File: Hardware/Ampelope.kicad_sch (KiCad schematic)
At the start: 44 parts, among them J1 Gate1_In, J3 Eurorack_10_pin_power, J4 Audio1_Out, U1 TL074

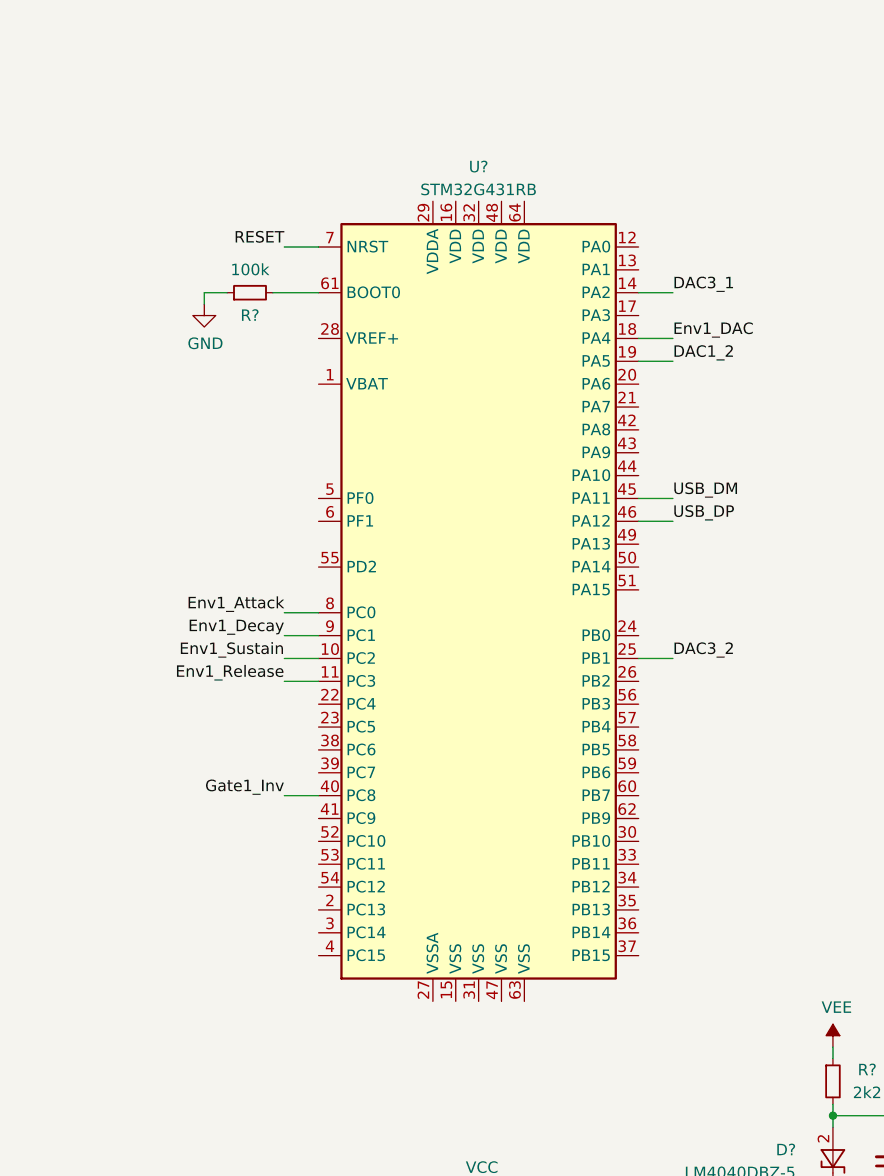
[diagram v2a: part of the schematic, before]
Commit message: Added power supply components to schematic
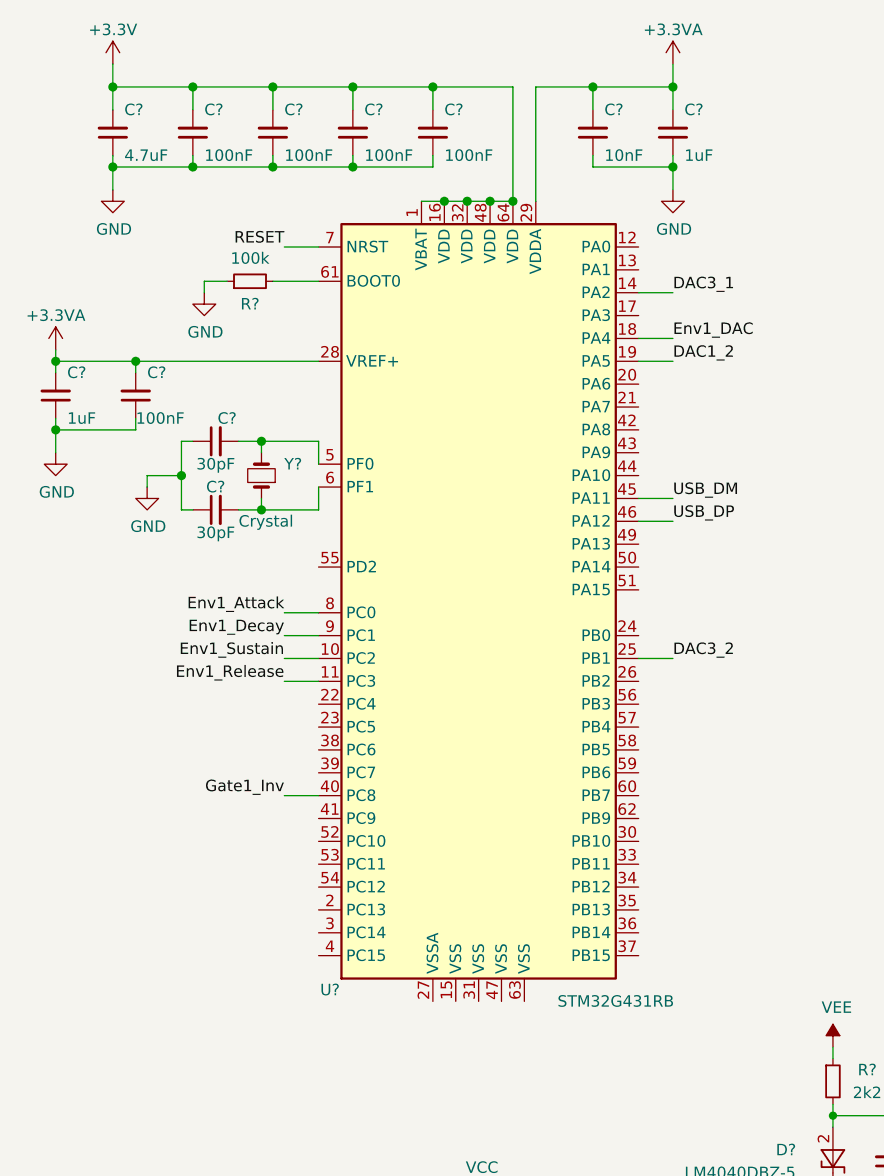
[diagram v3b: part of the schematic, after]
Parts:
- added C? (x5): 100nF, symbol Device:C_Small
- added C? (x2): 1uF, symbol Device:C_Small
- added C? (x2): 30pF, symbol Device:C_Small
- added C?: 10nF, symbol Device:C_Small
- added C?: 4.7uF, symbol Device:C_Small
- added Y?: Crystal, symbol Device:Crystal_Small
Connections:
- net +3.3VA: now also U?.28 (VREF+), U?.29 (VDDA), C?.2, C?.2, C?.2, C?.2
- net +3V3: now also U?.1 (VBAT), U?.16 (VDD), U?.32 (VDD), U?.48 (VDD), U?.64 (VDD), C?.2, C?.2, C?.2, C?.2, C?.2
- net GND: now also C?.1, C?.1, C?.1, C?.1, C?.1, C?.1, C?.1, C?.1, C?.1, C?.1, C?.1
- net at U?.5 (PF0): now also C?.2, Y?.2
- net at U?.6 (PF1): now also C?.2, Y?.1
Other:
- moved on the sheet: R?

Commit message: Duplicated IO for all four envelopes/VCAs
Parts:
- removed C?: 100nF, Capacitors_SMD:C_0603_HandSoldering, symbol Device:C_Small
- removed D?: LM4040DBZ-5, TO_SOT_Packages_SMD:SOT-23, symbol Reference_Voltage:LM4040DBZ-10
- removed J?: Audio1_In, Custom_Footprints:THONKICONN_hole, symbol thonkiconn:AudioJack2_Ground_Switch
- removed R? (x2): 10k, Resistors_SMD:R_0603_HandSoldering, symbol Device:R_Small
- removed R?: 2k2, Resistors_SMD:R_0603_HandSoldering, symbol Device:R_Small
- removed unit 1 of U1
- added C? (x3): 100pF, symbol Device:C_Small
- added D? (x3): LED, symbol Device:LED
- added J?: Audio1_In, Custom_Footprints:THONKICONN_hole, symbol thonkiconn:AudioJack2_Ground_Switch
- added J?: Audio2_In, Custom_Footprints:THONKICONN_hole, symbol thonkiconn:AudioJack2_Ground_Switch
- added J?: Audio4_Out, Custom_Footprints:THONKICONN_hole, symbol thonkiconn:AudioJack2_Ground_Switch
- added J?: Env3_Out, Custom_Footprints:THONKICONN_hole, symbol thonkiconn:AudioJack2_Ground_Switch
- added J?: Gate4_In, Custom_Footprints:THONKICONN_hole, symbol thonkiconn:AudioJack2_Ground_Switch
- added J?: Audio4_In, Custom_Footprints:THONKICONN_hole, symbol thonkiconn:AudioJack2_Ground_Switch
- added J?: Audio3_In, Custom_Footprints:THONKICONN_hole, symbol thonkiconn:AudioJack2_Ground_Switch
- added J?: Gate2_In, Custom_Footprints:THONKICONN_hole, symbol thonkiconn:AudioJack2_Ground_Switch
- added J?: Audio3_Out, Custom_Footprints:THONKICONN_hole, symbol thonkiconn:AudioJack2_Ground_Switch
- added J?: Env4_Out, Custom_Footprints:THONKICONN_hole, symbol thonkiconn:AudioJack2_Ground_Switch
- added J?: Env2_Out, Custom_Footprints:THONKICONN_hole, symbol thonkiconn:AudioJack2_Ground_Switch
- added J?: Audio2_Out, Custom_Footprints:THONKICONN_hole, symbol thonkiconn:AudioJack2_Ground_Switch
- added J?: Gate3_In, Custom_Footprints:THONKICONN_hole, symbol thonkiconn:AudioJack2_Ground_Switch
- added Q? (x3): 2N3904, Package_TO_SOT_THT:TO-92_Inline, symbol Transistor_BJT:2N3904
- added R? (x10): 1k, Resistors_SMD:R_0603_HandSoldering, symbol Device:R_Small
- added R? (x8): 10k, Resistors_SMD:R_0603_HandSoldering, symbol Device:R_Small
- added R? (x3): 30k, Resistors_SMD:R_0603_HandSoldering, symbol Device:R_Small
- added R? (x3): 75k, Resistors_SMD:R_0603_HandSoldering, symbol Device:R
- added R? (x3): 1k, Resistors_SMD:R_0603_HandSoldering, symbol Device:R
- added R? (x3): 20k, Resistors_SMD:R_0603_HandSoldering, symbol Device:R
- added R? (x3): 47k, Resistors_SMD:R_0603_HandSoldering, symbol Device:R
- added SW?: SW_SP3T, symbol Switch:SW_SP3T
- added U? (x12): TL074, Package_SO:SOIC-14_3.9x8.7mm_P1.27mm, symbol Amplifier_Operational:TL074
- J?: value Audio1_Out -> Env1_Out
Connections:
- net +3V3: now also R?.2, R?.2, R?.2
- net Audio1_In_Buff: now also R?.1, U?.1
- net Audio1_VCA: now also U1.2 (-); no longer U1.6 (-)
- net Audio2_In_Buff: now also R?.1, U?.7
- net Audio2_VCA: now also C?.1, R?.2, U?.6 (-)
- net Audio3_In_Buff: now also R?.1, U?.8
- net Audio3_VCA: now also C?.1, R?.2, U?.9 (-)
- net Audio4_In_Buff: now also R?.1, U?.14
- net Audio4_VCA: now also C?.1, R?.2, U?.13 (-)
- net DAC1_2: no longer U?.19 (PA5)
- net DAC3_1: no longer U?.14 (PA2)
- net DAC3_2: no longer U?.25 (PB1)
- net GND: now also U1.3 (+), U1.3 (+), U?.15 (VSS), U?.27 (VSSA), U?.31 (VSS), U?.47 (VSS), U?.63 (VSS), J?.1, J?.1, J?.1, J?.1, J?.1, J?.1, J?.1, J?.1, J?.1, J?.1, J?.1, J?.1, J?.1, J?.2, J?.2, J?.2, J?.2, J?.3, J?.3, J?.3, J?.3, Q?.1 (E), Q?.1 (E), Q?.1 (E), R?.2, R?.2, R?.2, R?.2, R?.2, R?.2, R?.2, U?.10 (+), U?.10 (+), U?.10 (+), U?.12 (+), U?.12 (+), U?.12 (+), U?.3 (+), U?.5 (+), U?.5 (+), U?.5 (+); no longer U1.10 (+), U1.5 (+)
- net VCC: now also U?.4 (V+), U?.4 (V+)
- net VEE: now also R?.2, R?.2, R?.2, U?.11 (V-), U?.11 (V-)
- net Gate1: now reaches J1.3, R?.1
- net Gate1: now also J?.2
- net at D?.2 (A), J?.3, R?.1: now also U1.1; no longer U1.8
- net at R?.1, R?.1, R?.2: now also U1.2 (-); no longer U1.9 (-)
- net at C?.2, R?.1: now also U1.1, R?.2; no longer J4.3, U1.7
- new net: Q?.2 (B), R?.2 (x3)
- new net: J?.3, R?.1 (x4)
- new net: C?.2, R?.1, R?.2, U?.8
- new net: R?.1, R?.2, U?.6 (-)
- new net: R?.1, R?.2, U?.2 (-)
- new net: R?.1, R?.2, U?.9 (-)
- new net: R?.1, R?.2, U?.13 (-)
- new net: D?.2 (A), J?.3, R?.1, U?.8
- new net: R?.1, R?.1, R?.2, U?.13 (-)
- new net: D?.2 (A), J?.3, R?.1, U?.14
- new net: D?.1 (K), R?.1 (x3)
- new net: R?.1, R?.1, R?.2, U?.9 (-)
- new net: C?.2, R?.1, R?.2, U?.7
- new net: D?.2 (A), J?.3, R?.1, U?.7
- new net: R?.1, R?.1, R?.2, U?.6 (-)
- new net: C?.2, R?.1, R?.2, U?.14
- new net: J4.3, R?.1
- new net Env2_DAC: R?.2, U?.19 (PA5)
- new net Env3_DAC: R?.2, U?.14 (PA2)
- new net Env4_DAC: R?.2, U?.25 (PB1)
- new net Gate2: J?.2, J?.3, R?.1
- new net Gate2_Inv: Q?.3 (C), R?.1
- new net Gate3: J?.2, J?.3, R?.1
- new net Gate3_Inv: Q?.3 (C), R?.1
- new net Gate4_Inv: Q?.3 (C), R?.1
- no-connect marks 4 -> 10
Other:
- moved on the sheet: C2, C3, C?, D1, D2, D?, J1, J3, J4, J?, L?, Q?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

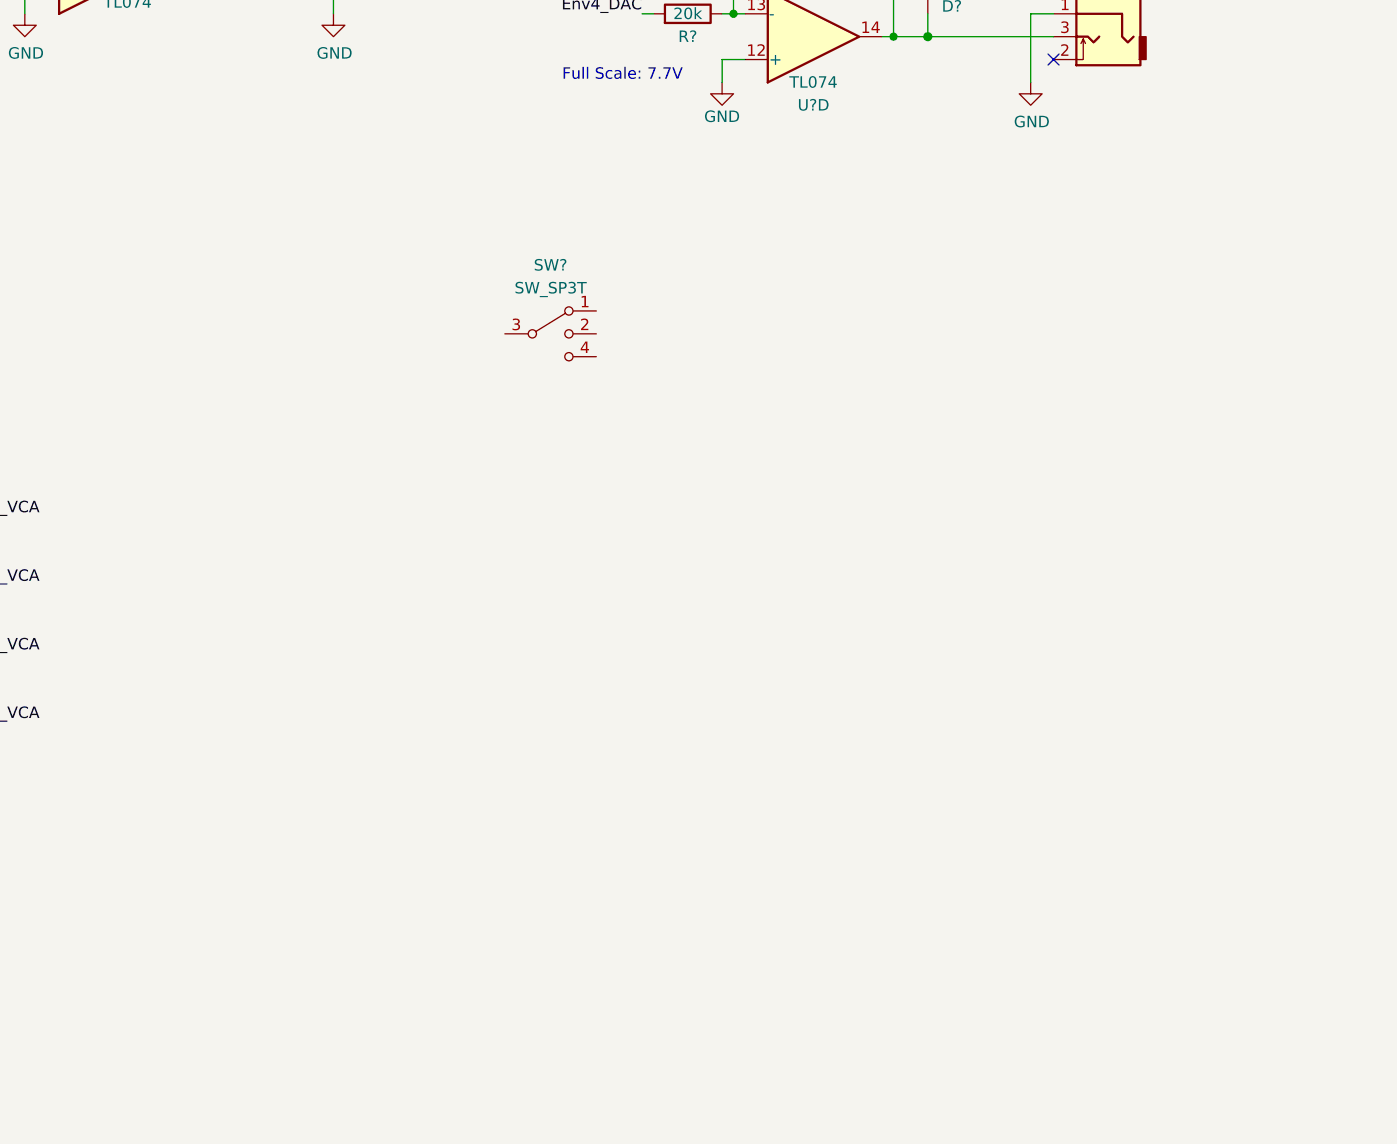
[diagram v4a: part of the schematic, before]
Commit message: Added switches and poteniometers to schematic
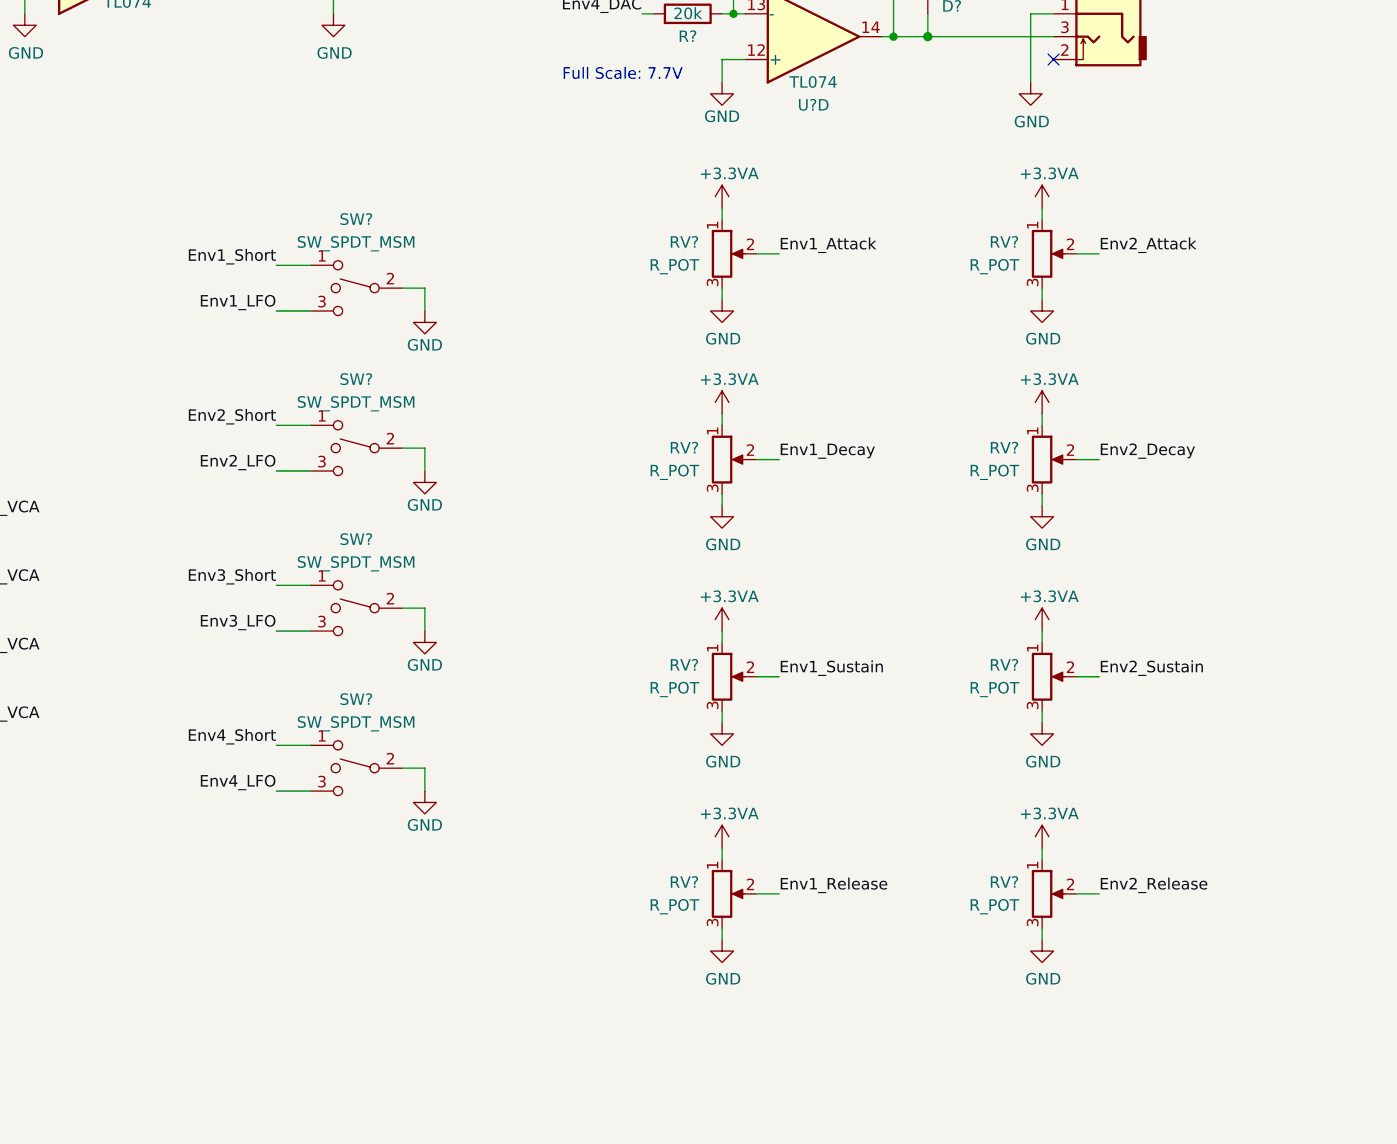
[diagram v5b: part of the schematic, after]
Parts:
- removed SW?: SW_SP3T, symbol Switch:SW_SP3T
- added RV? (x8): R_POT, symbol Encoder:R_POT
- added SW? (x4): SW_SPDT_MSM, symbol Switch:SW_SPDT_MSM
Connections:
- net +3.3VA: now also RV?.1, RV?.1, RV?.1, RV?.1, RV?.1, RV?.1, RV?.1, RV?.1
- net Env1_Attack: now also RV?.2
- net Env1_Decay: now also RV?.2
- net Env1_Release: now also RV?.2
- net Env1_Sustain: now also RV?.2
- net GND: now also RV?.3, RV?.3, RV?.3, RV?.3, RV?.3, RV?.3, RV?.3, RV?.3, SW?.2, SW?.2, SW?.2, SW?.2
- new net Env1_LFO: SW?.3
- new net Env1_Short: SW?.1
- new net Env2_Attack: RV?.2
- new net Env2_Decay: RV?.2
- new net Env2_LFO: SW?.3
- new net Env2_Release: RV?.2
- new net Env2_Short: SW?.1
- new net Env2_Sustain: RV?.2
- new net Env3_LFO: SW?.3
- new net Env3_Short: SW?.1
- new net Env4_LFO: SW?.3
- new net Env4_Short: SW?.1

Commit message: More work on schematic
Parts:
- removed Q? (x4): 2N3904, Package_TO_SOT_THT:TO-92_Inline, symbol Transistor_BJT:2N3904
- removed unit 4 of U1
- removed Y?: Crystal, symbol Device:Crystal_Small
- added C20: 10nF, Capacitors_SMD:C_0603_HandSoldering, symbol Device:C_Small
- added C21, C22: 100nF, Capacitors_SMD:C_0603_HandSoldering, symbol Device:C_Small
- added J18: SWD_Header, Custom_Footprints:SWD_header, symbol Connector:Conn_01x04_Male
- added J19: USB_B_Micro, Custom_Footprints:USB_Micro-B_Amphenol, symbol Connector:USB_B_Micro
- added Q1, Q2, Q3, Q4: MMBT3904, Package_TO_SOT_SMD:SOT-23, symbol Transistor_BJT:MMBT3904
- added R14: 100R, Resistors_SMD:R_0603_HandSoldering, symbol Device:R_Small
- added RESET1: SW_Push, Custom_Footprints:SW_PUSH_6mm_aligned, symbol Switch:SW_Push
- added RV5: R_POT, Custom_Footprints:Alpha_9mm_Potentiometer_Aligned, symbol Encoder:R_POT
- added Y1: 8MHz 20pF, Crystals:Crystal_SMD_5032-2pin_5.0x3.2mm_HandSoldering, symbol Device:Crystal
- C1, C11, C13, C14, C15, C2, C23, C24, C25, C26, C3, C5, C6, C7, C8: renamed from C?; footprint (none) -> Capacitors_SMD:C_0603_HandSoldering
- D3, D4, D5, D6: renamed from D?; footprint (none) -> LEDs:LED_D3.0mm
- L1: renamed from L?; footprint (none) -> Inductors_SMD:L_0805_HandSoldering
- RV1, RV2, RV3, RV4, RV6, RV7, RV8, RV9: renamed from RV?; footprint (none) -> Custom_Footprints:Alpha_9mm_Potentiometer_Aligned
- SW1, SW2, SW3, SW4: renamed from SW?; footprint (none) -> Custom_Footprints:SPDT_SubMiniature_Aligned
- U2: renamed from U?; value SSI2164 -> AS3364
- U3: renamed from U?; footprint (none) -> TO_SOT_Packages_SMD:SOT-223-3_TabPin2
- gave numbers to parts that had none: 73
- renumbered C3 to C10, C2 to C9, J3 to J1, J4 to J10, J1 to J2, U1 to U4, U1 to U5, U1 to U6
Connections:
- net +3.3VA: now also RV5.1
- net +3V3: now also J18.1 (Pin_1)
- net Env1_LFO: now also U1.56 (PB3)
- net Env1_Short: now also U1.26 (PB2)
- net Env2_Attack: now also U1.12 (PA0)
- net Env2_Decay: now also U1.13 (PA1)
- net Env2_LFO: now also U1.58 (PB5)
- net Env2_Release: now also U1.24 (PB0)
- net Env2_Short: now also U1.57 (PB4)
- net Env2_Sustain: now also U1.17 (PA3)
- net Env3_LFO: now also U1.60 (PB7)
- net Env3_Short: now also U1.59 (PB6)
- net Env4_LFO: now also U1.30 (PB10)
- net Env4_Short: now also U1.62 (PB9)
- net GND: now also C20.2, C21.2, C22.2, J18.2 (Pin_2), J19.5 (GND), Q1.2 (E), Q2.2 (E), Q3.2 (E), Q4.2 (E), RESET1.2, RV5.3
- net Gate1_Inv: now also U1.53 (PC11), Q1.3 (C)
- net Gate2_Inv: now also U1.41 (PC9), Q2.3 (C)
- net Gate3_Inv: now also U1.52 (PC10), Q3.3 (C)
- net Gate4_Inv: now also Q4.3 (C)
- net RESET: now also RESET1.1
- net USB_DM: now also J19.2 (D-)
- net USB_DP: now also J19.3 (D+)
- net VCC: now also C22.1
- net VEE: now also C21.1
- net at R13.2: now also Q4.1 (B)
- net at R12.2: now also Q3.1 (B)
- net at R10.2: now also Q1.1 (B)
- net at U2.1 (MODE): now also R14.2
- net at C6.2, U1.5 (PF0): now also Y1.2
- net at C7.2, U1.6 (PF1): now also Y1.1
- net at R11.2: now also Q2.1 (B)
- net LFO_Speed: now reaches U1.33 (PB11)
- net LFO_Speed: now also RV5.2
- net SWIO: now reaches U1.49 (PA13)
- net SWIO: now also J18.3 (Pin_3)
- net SWCLK: now reaches U1.50 (PA14)
- net SWCLK: now also J18.4 (Pin_4)
- new net: C20.1, R14.1
- new net USB_VBUS: J19.1 (VBUS)
- no-connect marks 10 -> 11
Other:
- moved on the sheet: C10, C12, C16, C17, C18, C19, C4, C9, D1, D2, J1, L1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
